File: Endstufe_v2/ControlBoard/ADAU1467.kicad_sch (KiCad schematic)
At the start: 40 parts, among them J10 DNP, J11 DNP, J12 DNP, U7 W25Q128JVS, U8 ADAU1467WBCPZ300, U9 ZPLR135_T8, Y2 24.576Mhz

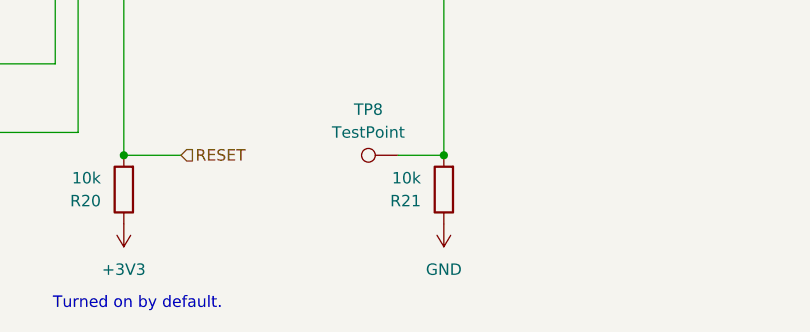
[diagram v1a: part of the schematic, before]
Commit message: Fix selfboot not being activated
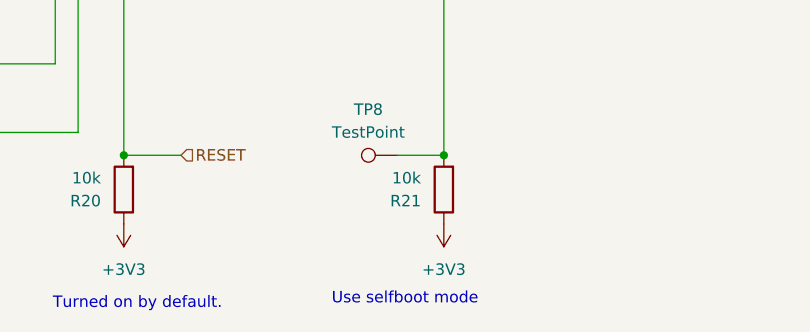
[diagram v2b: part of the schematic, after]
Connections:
- net +3V3: now also R21.1
- net GND: no longer R21.1
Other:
- note added: "Use selfboot mode"
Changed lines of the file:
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@@
 		)
 	)
+	(text "Use selfboot mode"
+		(exclude_from_sim no)
+		(at 164.592 189.992 0)
+		(effects
+			(font
+				(size 1.27 1.27)
+			)
+		)
+	)
 	(label "SPDIFIN"
 		(at 109.22 76.2 180)
@@
 	)
 	(symbol
+		(lib_id "Endstufe:+3V3")
+		(at 168.91 181.61 180)
+		(unit 1)
+		(exclude_from_sim no)
+		(in_bom yes)
+		(on_board yes)
+		(dnp no)
+		(fields_autoplaced yes)
+		(property "Reference" "#PWR066"
+			(at 168.91 177.8 0)
+			(effects
+				(font
+					(size 1.27 1.27)
+				)
+				(hide yes)
+			)
+		)
+		(property "Value" "+3V3"
+			(at 168.91 186.69 0)
+			(effects
+				(font
+					(size 1.27 1.27)
+				)
+			)
+		)
+		(property "Footprint" ""
+			(at 168.91 181.61 0)
+			(effects
+				(font
+					(size 1.27 1.27)
+				)
+				(hide yes)
+			)
+		)
+		(property "Datasheet" ""
+			(at 168.91 181.61 0)
+			(effects
+				(font
+					(size 1.27 1.27)
+				)
+				(hide yes)
+			)
+		)
+		(property "Description" ""
+			(at 168.91 181.61 0)
+			(effects
+				(font
+					(size 1.27 1.27)
+				)
+				(hide yes)
+			)
+		)
+		(pin "1"
+		)
+		(instances
+			(project "ControlBoard"
+				(path "/4f887f51-77c1-41d4-a3eb-45d362caffe1/70b67e3d-1dd9-4820-9634-6ce668eb2a07"
+					(reference "#PWR066")
+					(unit 1)
+				)
+			)
+		)
+	)
+	(symbol
 		(lib_id "Endstufe:GND")
 		(at 39.37 93.98 90)
@@
 					(unit 1)
 				)
-			)
-		)
-	)
-	(symbol
-		(lib_id "Endstufe:+3V3")
-		(at 168.91 181.61 180)
-		(unit 1)
-		(exclude_from_sim no)
-		(in_bom yes)
-		(on_board yes)
-		(dnp no)
-		(fields_autoplaced yes)
-		(property "Reference" "#PWR066"
-			(at 168.91 177.8 0)
-			(effects
-				(font
-					(size 1.27 1.27)
-				)
-				(hide yes)
-			)
-		)
-		(property "Value" "GND"
-			(at 168.91 186.69 0)
-			(effects
-				(font
-					(size 1.27 1.27)
-				)
-			)
-		)
-		(property "Footprint" ""
-			(at 168.91 181.61 0)
-			(effects
-				(font
-					(size 1.27 1.27)
-				)
-				(hide yes)
-			)
-		)
-		(property "Datasheet" ""
-			(at 168.91 181.61 0)
-			(effects
-				(font
-					(size 1.27 1.27)
-				)
-				(hide yes)
-			)
-		)
-		(property "Description" ""
-			(at 168.91 181.61 0)
-			(effects
-				(font
-					(size 1.27 1.27)
-				)
-				(hide yes)
-			)
-		)
-		(pin "1"
-		)
-		(instances
-			(project "ControlBoard"
-				(path "/4f887f51-77c1-41d4-a3eb-45d362caffe1/70b67e3d-1dd9-4820-9634-6ce668eb2a07"
-					(reference "#PWR066")
-					(unit 1)
-				)

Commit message: Change unavailable parts to available ones, optimise silkscreen, do via stiching
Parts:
- C23, C24: footprint Capacitor_SMD:C_0402_1005Metric -> Endstufe:C_0402_1005Metric
- C25, C26: LCSC Part # C458861 -> C526980
- J10: footprint Connector_PinHeader_2.54mm:PinHeader_2x03_P2.54mm_Vertical -> Endstufe:PinHeader_2x03_P2.54mm_Vertical
- J11: footprint Connector_PinHeader_2.54mm:PinHeader_1x04_P2.54mm_Vertical -> Endstufe:PinHeader_1x04_P2.54mm_Vertical
- J12: footprint Endstufe:CONN-TH_B4B-XH-2-LF-SN -> Endstufe:JST_XH_B4B-XH-A_1x04_P2.50mm_Vertical; JLCPCB Position Offset (none) -> 0,-0.5; LCSC (none) -> C157999
- L2: footprint Inductor_SMD:L_0805_2012Metric -> Endstufe:L_0805_2012Metric
- R18: LCSC Part # (none) -> C4275
- TP3, TP4, TP5, TP6, TP7, TP8: footprint TestPoint:TestPoint_Pad_D1.0mm -> Endstufe:TestPoint_Pad_D1.0mm
- U9: footprint CONN-TH_ZPLR135-T8 -> Endstufe:CONN-TH_ZPLR135-T8; JLCPCB Position Offset (none) -> 0,-3
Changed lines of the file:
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@@
 			)
 		)
-		(property "Footprint" "TestPoint:TestPoint_Pad_D1.0mm"
+		(property "Footprint" "Endstufe:TestPoint_Pad_D1.0mm"
 			(at 146.05 46.99 0)
 			(effects
@@
 			)
 		)
-		(property "LCSC Part #" "C458861"
+		(property "LCSC Part #" "C526980"
 			(at 93.98 160.02 0)
 			(effects
@@
 			)
 		)
-		(property "Footprint" "Connector_PinHeader_2.54mm:PinHeader_1x04_P2.54mm_Vertical"
+		(property "Footprint" "Endstufe:PinHeader_1x04_P2.54mm_Vertical"
 			(at 166.37 29.21 0)
 			(effects
@@
 			)
 		)
-		(property "Footprint" "TestPoint:TestPoint_Pad_D1.0mm"
+		(property "Footprint" "Endstufe:TestPoint_Pad_D1.0mm"
 			(at 109.22 91.44 0)
 			(effects
@@
 			)
 		)
-		(property "Footprint" "TestPoint:TestPoint_Pad_D1.0mm"
+		(property "Footprint" "Endstufe:TestPoint_Pad_D1.0mm"
 			(at 148.59 46.99 0)
 			(effects
@@
 			)
 		)
-		(property "Footprint" "TestPoint:TestPoint_Pad_D1.0mm"
+		(property "Footprint" "Endstufe:TestPoint_Pad_D1.0mm"
 			(at 163.83 168.91 0)
 			(effects
@@
 			)
 		)
-		(property "Footprint" "CONN-TH_ZPLR135-T8"
+		(property "Footprint" "Endstufe:CONN-TH_ZPLR135-T8"
 			(at 256.54 99.06 0)
 			(effects
@@
 			)
 		)
+		(property "JLCPCB Position Offset" "0,-3"
+			(at 0 177.8 0)
+			(effects
+				(font
+					(size 1.27 1.27)
+				)
+				(hide yes)
+			)
+		)
 		(pin "4"
 		)
@@
 			)
 		)
-		(property "Footprint" "Endstufe:CONN-TH_B4B-XH-2-LF-SN"
+		(property "Footprint" "Endstufe:JST_XH_B4B-XH-A_1x04_P2.50mm_Vertical"
 			(at 208.28 116.84 0)
 			(effects
@@
 			)
 		)
+		(property "JLCPCB Position Offset" "0,-0.5"
+			(at 416.56 0 0)
+			(effects
+				(font
+					(size 1.27 1.27)
+				)
+				(hide yes)
+			)
+		)
+		(property "LCSC" "C157999"
+			(at 416.56 0 0)
+			(effects
+				(font
+					(size 1.27 1.27)
+				)
+				(hide yes)
+			)
+		)
 		(pin "2"
 		)
@@
 			)
 		)
-		(property "Footprint" "Inductor_SMD:L_0805_2012Metric"
+		(property "Footprint" "Endstufe:L_0805_2012Metric"
 			(at 247.65 100.33 0)
 			(effects
@@
 			)
 		)
-		(property "LCSC Part #" "C458861"
+		(property "LCSC Part #" "C526980"
 			(at 93.98 175.26 0)
 			(effects
@@
 			)
 		)
-		(property "Footprint" "TestPoint:TestPoint_Pad_D1.0mm"
+		(property "Footprint" "Endstufe:TestPoint_Pad_D1.0mm"
 			(at 125.73 143.51 0)
 			(effects
@@
 			)
 		)
-		(property "Footprint" "TestPoint:TestPoint_Pad_D1.0mm"
+		(property "Footprint" "Endstufe:TestPoint_Pad_D1.0mm"
 			(at 62.23 83.82 0)
 			(effects
@@
 			)
 		)
-		(property "Footprint" "Capacitor_SMD:C_0402_1005Metric"
+		(property "Footprint" "Endstufe:C_0402_1005Metric"
 			(at 86.0552 118.11 0)
 			(effects
@@
 			)
 		)
-		(property "Footprint" "Capacitor_SMD:C_0402_1005Metric"
+		(property "Footprint" "Endstufe:C_0402_1005Metric"
 			(at 80.01 109.5248 0)
 			(effects
@@
 			)
 		)
+		(property "LCSC Part #" "C4275"
+			(at 194.31 194.31 0)
+			(effects
+				(font
+					(size 1.27 1.27)
+				)
+				(hide yes)
+			)
+		)
 		(pin "2"
 		)
@@
 			)
 		)
-		(property "Footprint" "Connector_PinHeader_2.54mm:PinHeader_2x03_P2.54mm_Vertical"
+		(property "Footprint" "Endstufe:PinHeader_2x03_P2.54mm_Vertical"
 			(at 31.75 97.79 0)
 			(effects
